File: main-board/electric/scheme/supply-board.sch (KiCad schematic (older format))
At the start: 128 parts

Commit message: Board scheme development...
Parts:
- removed C? (x3): 100n, symbol C
- removed D?: AD8607, symbol AD8607
- removed D?: 1Nxxxx, symbol DIODESCH
- removed K? (x2): i2c-1, symbol CONN_3
- removed P? (x4): PWR-IN, symbol CONN_2
- removed P?: CONN_4, symbol CONN_4
- removed R? (x5): 1, symbol R
- removed R?: 65k, symbol R
- removed R? (x2): 10k, symbol R
- removed R? (x4): 30k, symbol R
- removed R? (x2): 50, symbol R
- removed R?: 100k, symbol R
- added C? (x2): 4u7, ~, symbol C
- added P?: CONN_3X2, symbol CONN_3X2
- added P?: PWR-IN, symbol CONN_2
- added P? (x5): TST, ~, symbol TST
- added P?: CONN_10, symbol CONN_10
- added P?: CONN_4, symbol CONN_4
- added R? (x4): 2k, symbol R
- added R? (x3): 10k, symbol R
- added R? (x9): 30k, symbol R
- added R? (x5): 1, symbol R
- R? (x2): value 10k -> 1k
- R? (x2): value 50 -> 10
- R? (x2): value 500 -> 1k
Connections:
- net labels added: batt-volt, boost+, boost-current, buck-current, buck-volt, in2+, in2-, solar+, solar-volt
- wire segments 391 -> 396
- no-connect marks 12 -> 15
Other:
- note added: "Battery connection socket."
- note added: "Cross board communication socket.\nThere is one at this board. But there should \nbe two neighbour such sockets on all other \nboards to be able to stack them together."
- note added: "Power source such as solar panel.\nIt's voltage shouldn't be greater then \nbattery's voltage. It is because \nbattery is changed using boost \nscheme."
- note added: "Programming socket is planned to be made of \nindividual pads. And programming cable is \nsupposed to be attached with crocodile clip."
- note added: "Socket for powering external devices."
- note added: "Two unconnected pins for screws.\nThe newest Raspberry Pi contains \nholes for M3 screws."
- note removed: "At zero frequency gain is (R28+R27)/R27.\nAim is to get +/-1.5Volts as current 2A.\nIf shunt resistors set resistance is 0.1Ohm\nthen they give 0.2V at 2A current.\nAmplification is 1.5/0.2 = 7.5.\nIf R27 = 10k.\nThen 7.5 = 1 + R28/10k.\nR28 = 10k * 6.5 = 65k."
- note removed: "Battery socket"
- note removed: "For powering GPS in standby mode."
- note removed: "There is an error here. Feed back should connect negative \nterminal with "ground" (here ref voltage instead of ground) \nthrough resistance. But here it connects output with ref \nvoltage. It is why output doesn't change."
- note removed: "Unspecified power source \nsuch as solar panel."
- note removed: "Vcc and tested close to Gnd voltage \nare summed in equal proportions. \nResult is close to Vcc/2."
- moved on the sheet: D?, P?, R?

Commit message: More or less finished schema.
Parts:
- added P?: PWR-IN, symbol CONN_2
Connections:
- net labels added: boost-volt, rx, temperature, tx
- net labels removed: VBus, boost-fb, buck-fb, current-fb, solar-fb, v-temp
- wire segments 396 -> 407
- no-connect marks 15 -> 9
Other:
- note added: "Optionally could be USB powered"
- note added: "This capacitor gives cutoff frequency at about 170kHz."
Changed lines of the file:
@@
 Sheet 1 1
 Title ""
-Date "17 aug 2013"
+Date "19 aug 2013"
 Rev ""
 Comp ""
@@
 Analog \ntemperature\nsensor
 Text Label 14100 4450 0    60   ~ 0
-v-temp
+buck-current
 Text Label 2300 11100 0    60   ~ 0
-v-temp
+temperature
 $Comp
 L GND #PWR?
@@
 	1    0    0    -1
 $EndComp
-Text Label 14200 5250 0    60   ~ 0
+Text Label 14000 9550 0    60   ~ 0
 moto4
-Text Label 14200 5050 0    60   ~ 0
+Text Label 14000 9750 0    60   ~ 0
 moto3
-Text Label 14200 4850 0    60   ~ 0
+Text Label 13950 8750 0    60   ~ 0
 moto2
-Text Label 14200 5450 0    60   ~ 0
+Text Label 13950 8550 0    60   ~ 0
 moto1
-Text Label 14100 4650 0    60   ~ 0
+Text Label 14100 2750 0    60   ~ 0
 moto-en
 Text Label 22350 12500 0    60   ~ 0
@@
 	-1   0    0    -1
 $EndComp
-NoConn ~ 13650 3050
 Text Label 14100 4250 0    60   ~ 0
-current-fb
+boost-current
 Text Label 18650 3400 1    60   ~ 0
 buck-out-5v
@@
 boost-pwm
 Text Label 14100 4050 0    60   ~ 0
-buck-fb
+buck-volt
 Text Label 14100 3850 0    60   ~ 0
-boost-fb
+boost-volt
 Text Label 14100 3650 0    60   ~ 0
-solar-fb
+solar-volt
 Text Label 24150 6550 1    60   ~ 0
 solar
@@
 	1    0    0    -1
 $EndComp
-NoConn ~ 9050 7050
-NoConn ~ 9050 6350
 Text Label 13950 8350 0    60   ~ 0
 sda-rpi
@@
 NoConn ~ 13650 6850
 NoConn ~ 13650 6650
-NoConn ~ 13650 6450
 $Comp
 L GND #PWR?
@@
 	0    -1   -1   0
 $EndComp
-Text Label 14100 9750 0    60   ~ 0
-led2
-Text Label 14100 9550 0    60   ~ 0
+Text Label 8400 6350 0    60   ~ 0
 led1
 Text Label 13950 9150 0    60   ~ 0
@@
 	1    0    0    -1
 $EndComp
-NoConn ~ 13650 8550
-NoConn ~ 13650 8750
 NoConn ~ 13650 7600
-NoConn ~ 13650 7400
-NoConn ~ 13650 2750
 $Comp
 L GND #PWR?
@@
 	1    0    0    -1
 $EndComp
-Text HLabel 29350 18400 1    60   Input ~ 0
-VBus
 $Comp
 L R R?
@@
 Text Notes 950  17200 0    60   ~ 0
 Socket for powering external devices.
+Wire Wire Line
+	13650 7400 14350 7400
+Text Label 14000 7400 0    60   ~ 0
+temperature
+Wire Wire Line
+	9050 6350 8350 6350
+Wire Wire Line
+	9050 7050 8350 7050
+Text Label 8400 7050 0    60   ~ 0
+led2
+Wire Wire Line
+	13650 6450 14350 6450
+Text Label 14000 6450 0    60   ~ 0
+usb-connected
+Text Label 14400 5250 0    60   ~ 0
+d-
+Text Label 14400 5450 0    60   ~ 0
+d+
+Wire Wire Line
+	13650 2750 14500 2750
+Wire Wire Line
+	13650 3050 14500 3050
+Wire Wire Line
+	13650 8550 14300 8550
+Wire Wire Line
+	13650 8750 14300 8750
+Text Label 14400 4850 0    60   ~ 0
+tx
+Text Label 14400 5050 0    60   ~ 0
+rx
+NoConn ~ 14500 3050
+NoConn ~ 14500 4650
+$Comp
+L CONN_2 P?
+U 1 1 5212922E
+P 29450 18050
+F 0 "P?" V 29400 18050 40  0000 C CNN
+F 1 "PWR-IN" V 29500 18050 40  0000 C CNN
+F 2 "" H 29450 18050 60  0001 C CNN
+F 3 "" H 29450 18050 60  0001 C CNN
+	1    29450 18050
+	0    -1   -1   0
+$EndComp
+Wire Wire Line
+	29550 18400 29550 18500
+Wire Wire Line
+	29550 18500 29850 18500
+Wire Wire Line
+	29850 18500 29850 17850
+Text Label 29850 18100 1    60   ~ 0
+batt+
+Text Notes 28900 17750 0    60   ~ 0
+Optionally could be USB powered
+Text Notes 13550 13400 0    60   ~ 0
+This capacitor gives cutoff frequency at about 170kHz.
+Text Notes 13900 19050 0    60   ~ 0
+This capacitor gives cutoff frequency at about 170kHz.
 $EndSCHEMATC

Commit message: Started placing components.
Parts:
- added K1: CONN_3, symbol CONN_3
- gave numbers to parts that had none: 134
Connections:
- net labels removed: boost-volt, out2+, out2-
- wire segments 407 -> 413

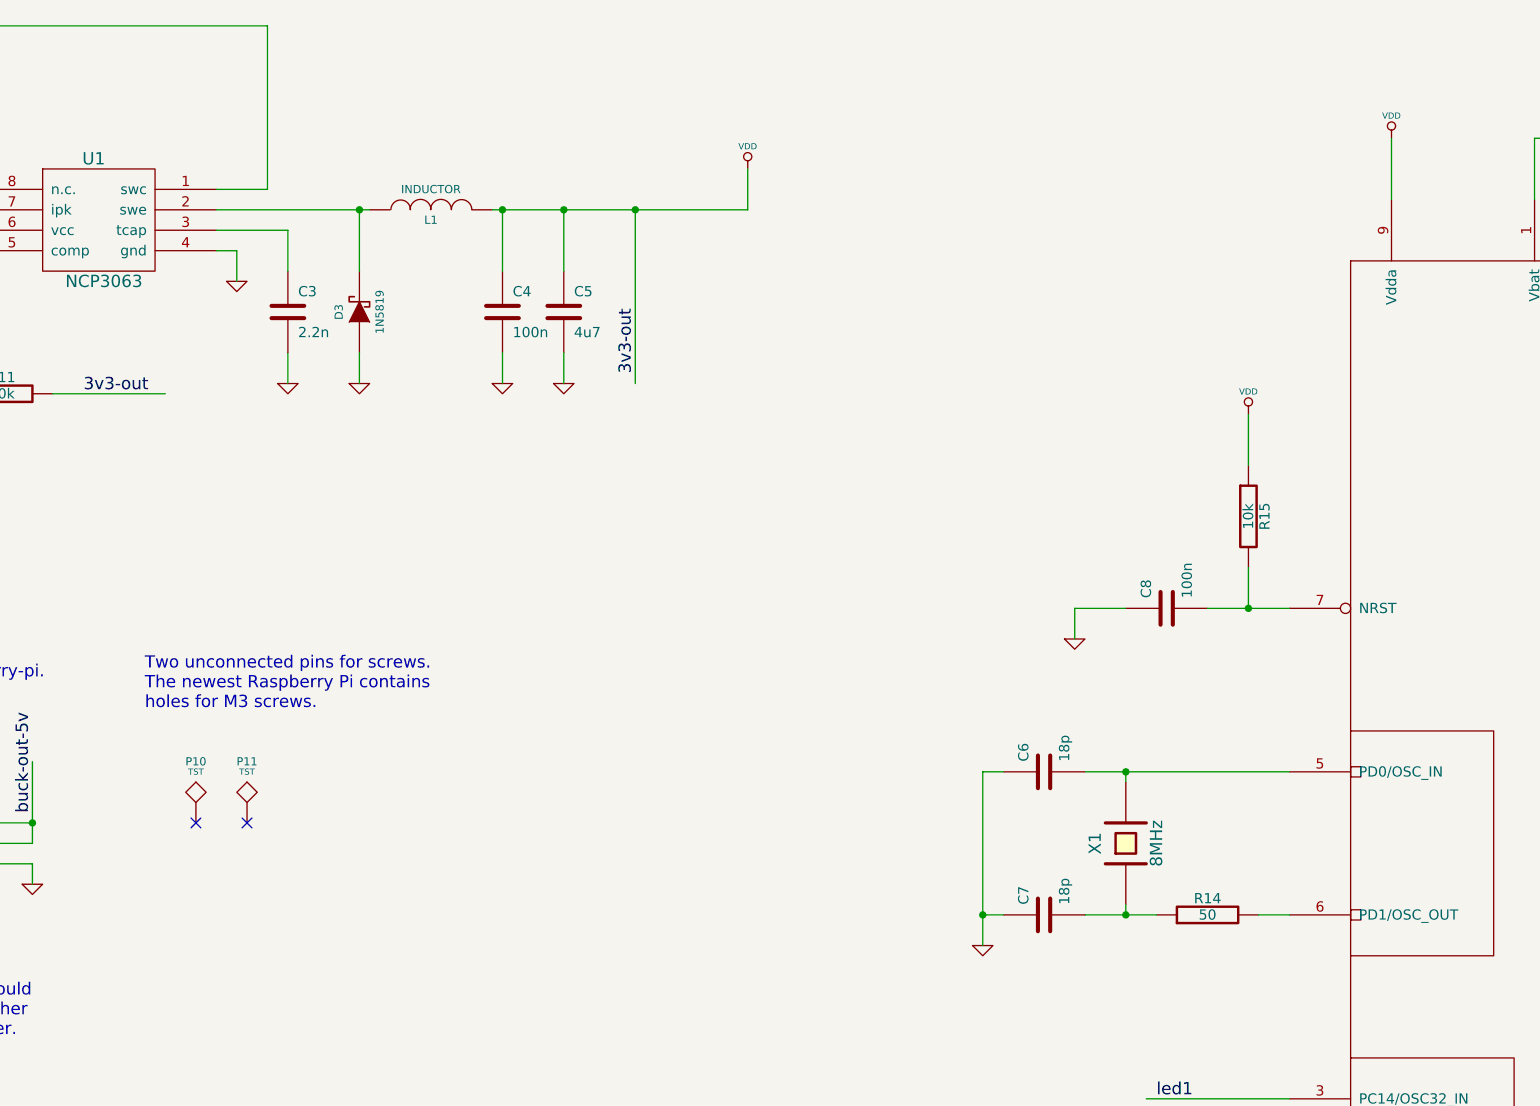
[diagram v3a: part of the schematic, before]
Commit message: Made footprints for components I didn't have footprints. And started placing components.
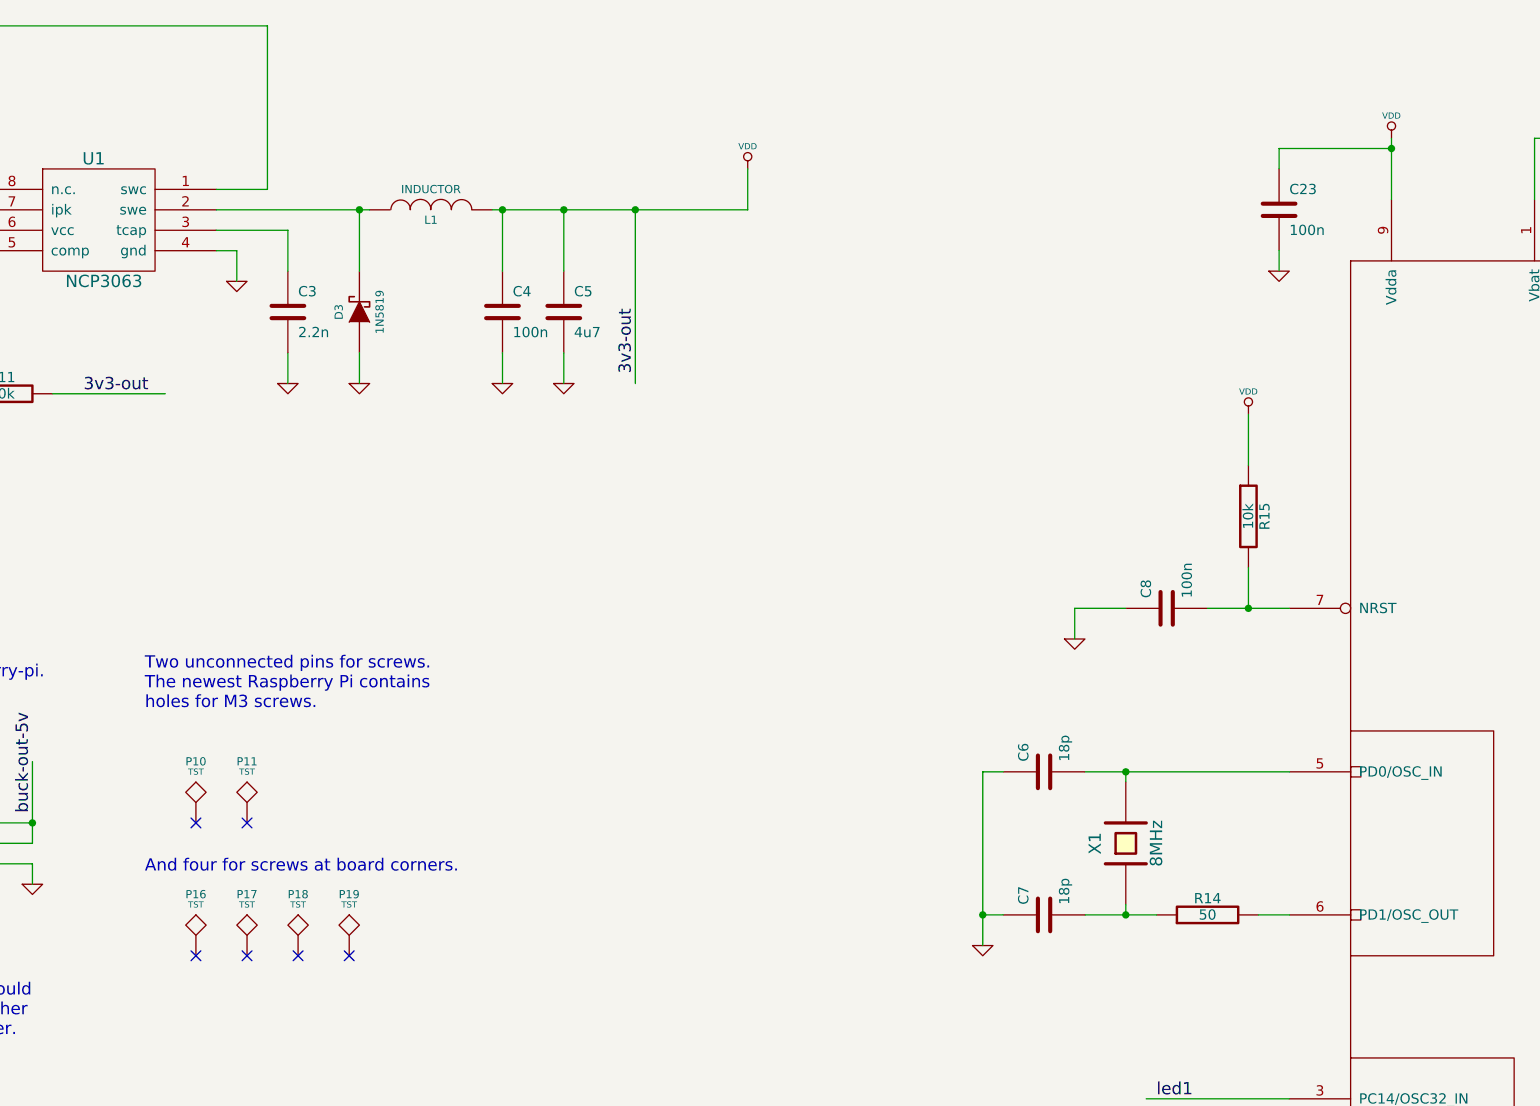
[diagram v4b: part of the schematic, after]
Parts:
- added C23: 100n, symbol C
- added P16, P17, P18, P19: TST, ~, symbol TST
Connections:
- wire segments 413 -> 416
- no-connect marks 9 -> 13
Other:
- note added: "And four for screws at board corners."

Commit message: Placing elements.
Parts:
- removed P15: CONN_4, symbol CONN_4
- R12, R13: value 10k -> 30k
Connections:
- wire segments 416 -> 410
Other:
- note removed: "5V for powering raspberry-pi, \n3G modem, camera and so on..."
